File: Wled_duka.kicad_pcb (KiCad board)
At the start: 2 copper layers, 100 x 100 mm, 41 parts, among them J1 7775-2, J2 DATA channels, J3 CH1&2, J4 CH3&4, J5 Relay out, J6 DMX512, J7 7775-2, J8 Vin_alt, Q1 AO3400A, U1 XL1509-5.0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

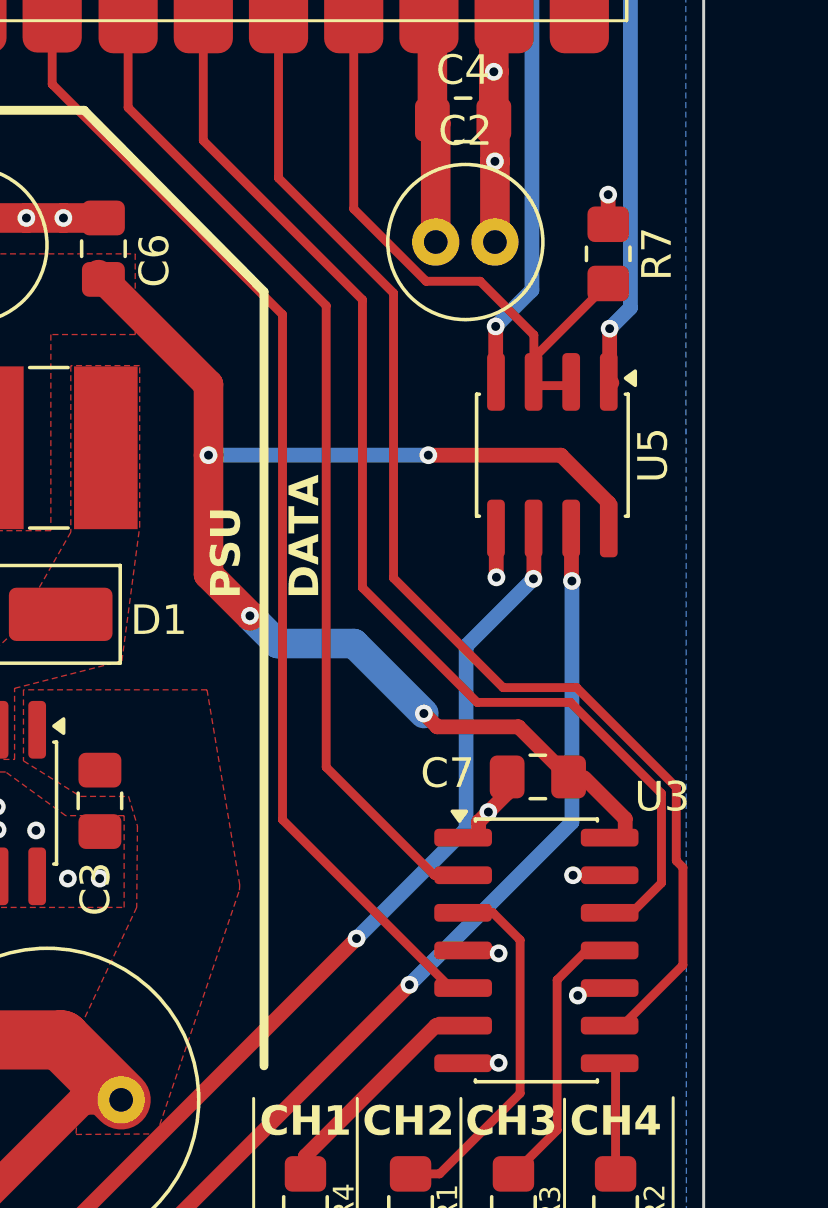
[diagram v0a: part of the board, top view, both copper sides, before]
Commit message: Pullup and Pulldown resistors, 3,3V for max3485
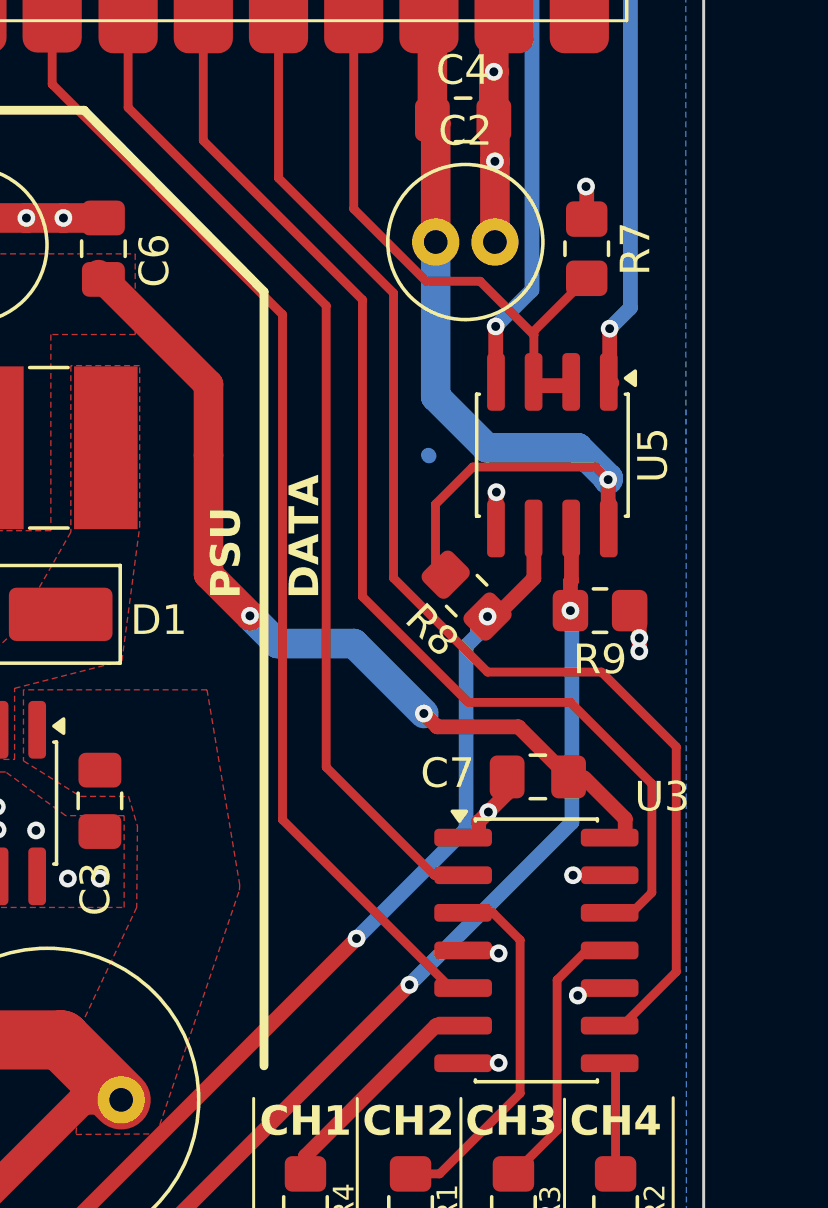
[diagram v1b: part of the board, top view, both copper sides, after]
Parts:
- added R8: 10k, Resistor_SMD:R_0805_2012Metric_Pad1.20x1.40mm_HandSolder, F.Cu at (158.6, 119.5)
- added R9: 10k, Resistor_SMD:R_0805_2012Metric_Pad1.20x1.40mm_HandSolder, F.Cu at (163.1, 120.0)
- moved R7 0.75 mm to (162.7, 107.8)
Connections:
- C2 pad 1: Net-(U2-3,3V) -> +3,3V
- C4 pad 1: Net-(U2-3,3V) -> +3,3V
- U2 pad 16: Net-(U2-3,3V) -> +3,3V
- U5 pad 8: +5V -> +3,3V
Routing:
- net +3,3V: track 0.00 -> 31.5 mm, vias 0 -> 1
- net +5V: track 91.3 -> 76.1 mm, vias 4 -> 2
- net Net-(U2-3,3V): track 7.97 -> 0.00 mm
- net GND: track 27.4 -> 28.5 mm, vias 27 -> 29
- net INT: track 21.1 -> 20.3 mm
- net IO_ch4: track 42.7 -> 43.3 mm

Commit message: Mouser.com ready components
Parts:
- removed D1: SS34, Diode_SMD:D_SMA_Handsoldering
- removed U5: MAX3485, Package_SO:SOIC-8_3.9x4.9mm_P1.27mm
- added C10: 100n, Capacitor_SMD:C_0805_2012Metric_Pad1.18x1.45mm_HandSolder, F.Cu at (146.9, 122.8)
- added C8: 22uF, Capacitor_SMD:C_1210_3225Metric_Pad1.33x2.70mm_HandSolder, F.Cu at (145.3, 110.9)
- added C9: 10uF, Capacitor_SMD:C_0805_2012Metric_Pad1.18x1.45mm_HandSolder, F.Cu at (142.6, 130.0)
- added D6: LED, LED_SMD:LED_0805_2012Metric_Pad1.15x1.40mm_HandSolder, F.Cu at (149.2, 128.3)
- added R10: 330, Resistor_SMD:R_0805_2012Metric_Pad1.20x1.40mm_HandSolder, F.Cu at (149.2, 132.6)
- added U4: ESP32_S3_supermini, Library:ESP32_S3_supermini, F.Cu at (153.5, 91.4)
- C1: value 470uF -> 100uF; footprint Capacitor_THT:C_Radial_D10.0mm_H16.0mm_P5.00mm -> Capacitor_THT:C_Radial_D5.0mm_H11.0mm_P2.00mm
- C2: value 220uF -> 100uF
- C3: value 100n -> 10uF
- C5: value 220uF -> 22uF; footprint Capacitor_THT:C_Radial_D5.0mm_H11.0mm_P2.00mm -> Capacitor_SMD:C_1210_3225Metric_Pad1.33x2.70mm_HandSolder
- L1: value 68uH -> 10uH; footprint Inductor_SMD:L_Ferrocore_DLG-0504 -> Inductor_SMD:L_Bourns_SRN6045TA
- Q1: value AO3400A -> DMN3067L-7
- R5: value 68R -> 62R
- TH1: footprint Resistor_THT:R_Axial_DIN0204_L3.6mm_D1.6mm_P5.08mm_Vertical -> Resistor_SMD:R_1206_3216Metric_Pad1.30x1.75mm_HandSolder
- U1: value XL1509-5.0 -> ADM3485xR
- U2: value ESP32_S3_supermini -> LMR51420; footprint sajat:ESP32_S3_supermini -> Package_TO_SOT_SMD:SOT-23-6_Handsoldering
- moved U2 35.1 mm to (143.2, 124.8), turned to 0 degrees
- moved C6 32.9 mm to (162.7, 79.3), turned to 0 degrees
- moved C2 32.2 mm to (155.1, 75.5)
- moved C4 24.2 mm to (158.8, 79.3)
- moved U1 22.6 mm to (161.5, 114.8)
- moved C1 5.83 mm to (141.7, 134.0), turned to 0 degrees
- moved L1 4.26 mm to (142.5, 118.3), turned to 90 degrees
- moved C3 3.85 mm to (142.6, 127.7), turned to 180 degrees
- moved TH1 3.45 mm to (134.2, 135.2)
- moved C5 2.19 mm to (141.9, 110.9)
- moved R7 1.75 mm to (160.9, 108.1)
- moved D4 1.26 mm to (132.4, 143.2)
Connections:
- L1 pad 1: Net-(D1-K) -> Net-(U2-SW)
- U1 pad 1: V12 -> RO RX
- U1 pad 2: Net-(D1-K) -> INT
- U1 pad 3: +5V -> INT
- U1 pad 4: GND -> DI TX
- U1 pad 6: GND -> Net-(D5-A1)
- U1 pad 7: GND -> Net-(D3-A1)
- U1 pad 8: GND -> +3,3V
- U2 pad 1: unconnected-(U2-RX-Pad1) -> GND
- U2 pad 2: unconnected-(U2-TX-Pad2) -> Net-(U2-SW)
- U2 pad 3: unconnected-(U2-GP1-Pad3) -> V12
- U2 pad 4: unconnected-(U2-GP2-Pad4) -> +5V
- U2 pad 5: unconnected-(U2-GP3-Pad5) -> V12
- U2 pad 6: unconnected-(U2-GP4-Pad6) -> Net-(U2-CB)
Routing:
- net DI TX: track 56.5 -> 22.7 mm
- net RO RX: track 53.5 -> 24.8 mm
- net +3,3V: track 31.5 -> 58.0 mm, vias 1 -> 4
- net +5V: track 76.1 -> 99.9 mm
- net GND: track 28.5 -> 34.3 mm, vias 29 -> 50
- net REL: track 44.6 -> 49.4 mm
- net INT: track 20.3 -> 16.4 mm
- net Net-(U2-CB): track 0.00 -> 2.33 mm
- net Net-(D6-K): track 0.00 -> 2.18 mm
- net IO_ch1: track 39.1 -> 37.8 mm
- net IO_ch2: track 34.5 -> 33.3 mm
- net IO_ch3: track 39.9 -> 38.6 mm
- net IO_ch4: track 43.3 -> 42.1 mm
- net V12: track 32.9 -> 34.0 mm, vias 0 -> 2
- net Net-(D2-K): track 4.49 -> 3.78 mm
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- added copper zone on F.Cu, net Net-(U2-SW)
- removed copper zone on F.Cu, net Net-(D1-K)
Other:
- board text added: "<----HIBÁS lábkiosztás!!!!!"
- board text added: "Power LED"
